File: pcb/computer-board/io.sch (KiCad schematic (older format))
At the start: 20 parts, among them J2 Conn_02x40_Odd_Even, J7 Conn_02x40_Odd_Even, U5 SN74AVC16T245DGGR, U6 SN74AVC4T245PWR, U7 74LVC1G14GW,125

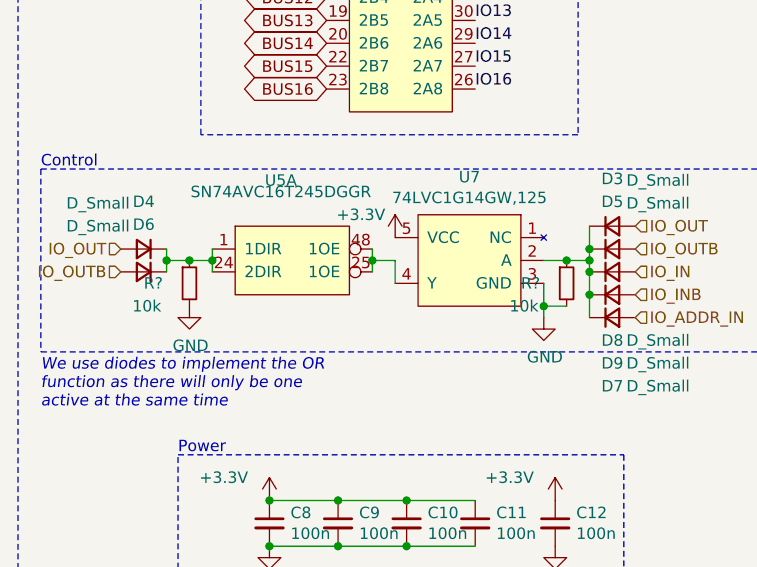
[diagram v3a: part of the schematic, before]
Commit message: added pulldowns on diode logic
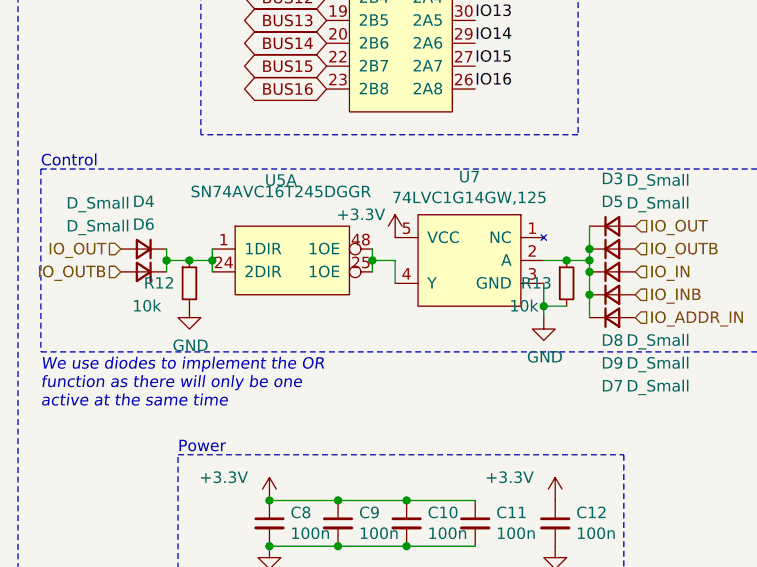
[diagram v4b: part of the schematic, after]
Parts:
- gave numbers to parts that had none: 2
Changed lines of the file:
@@
 P 1500 3600
 AR Path="/60033A38" Ref="R?"  Part="1"
-AR Path="/5F8B5DB4/60033A38" Ref="R?"  Part="1"
-F 0 "R?" H 1300 3600 50  0000 L CNN
+AR Path="/5F8B5DB4/60033A38" Ref="R12"  Part="1"
+F 0 "R12" H 1300 3600 50  0000 L CNN
 F 1 "10k" H 1250 3500 50  0000 L CNN
 F 2 "Resistor_SMD:R_0402_1005Metric_Pad0.72x0.64mm_HandSolder" H 1500 3600 50  0001 C CNN
@@
 P 3150 3600
 AR Path="/6004A131" Ref="R?"  Part="1"
-AR Path="/5F8B5DB4/6004A131" Ref="R?"  Part="1"
-F 0 "R?" H 2950 3600 50  0000 L CNN
+AR Path="/5F8B5DB4/6004A131" Ref="R13"  Part="1"
+F 0 "R13" H 2950 3600 50  0000 L CNN
 F 1 "10k" H 2900 3500 50  0000 L CNN
 F 2 "Resistor_SMD:R_0402_1005Metric_Pad0.72x0.64mm_HandSolder" H 3150 3600 50  0001 C CNN
@@
 P 1500 3700
 AR Path="/5F95DC76/6010C509" Ref="#PWR?"  Part="1"
-AR Path="/5F8B5DB4/6010C509" Ref="#PWR?"  Part="1"
-F 0 "#PWR?" H 1500 3450 50  0001 C CNN
+AR Path="/5F8B5DB4/6010C509" Ref="#PWR0171"  Part="1"
+F 0 "#PWR0171" H 1500 3450 50  0001 C CNN
 F 1 "GND" H 1505 3527 50  0000 C CNN
 F 2 "" H 1500 3700 50  0001 C CNN
